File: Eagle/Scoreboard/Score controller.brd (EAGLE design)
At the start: 80 x 40.6 mm, 21 parts, among them IC3 74HC595N, Q1 BD437, Q2 BD437, Q3 BD437, Q4 BD437, Q5 BD437, Q6 BD437, Q7 BD437

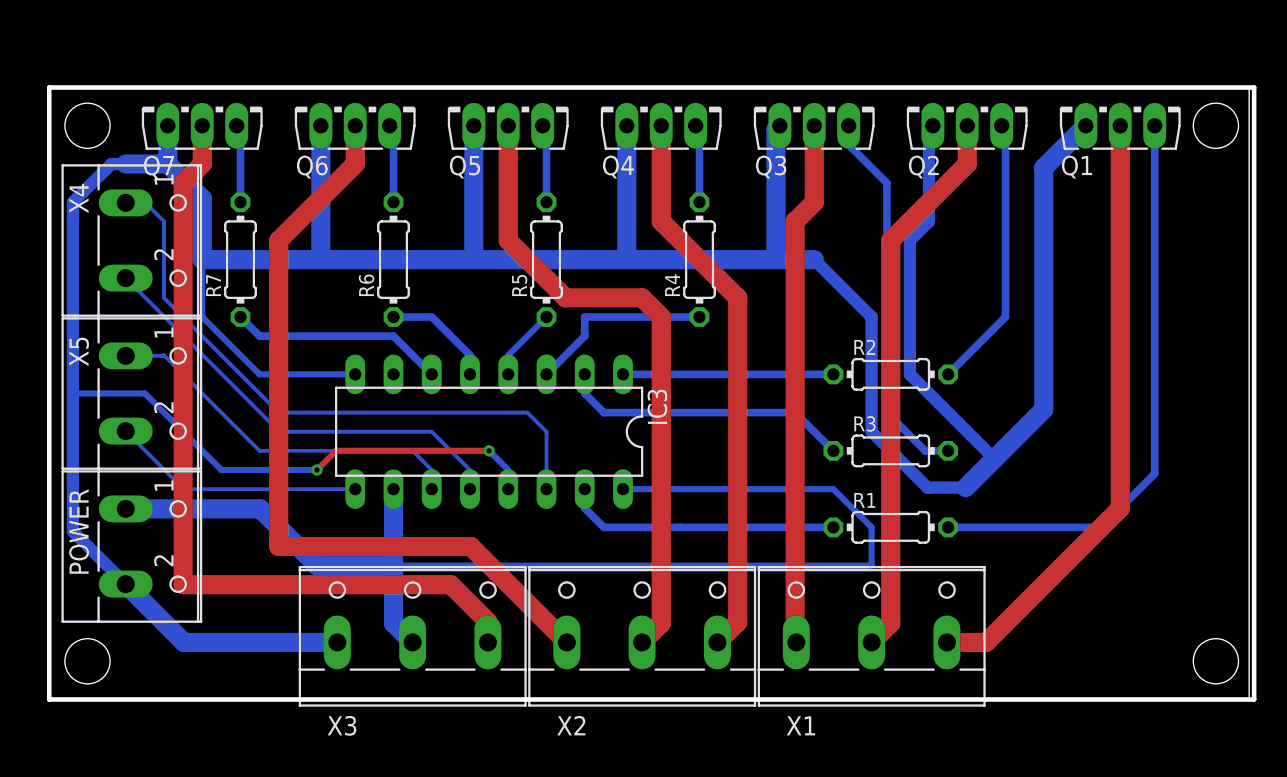
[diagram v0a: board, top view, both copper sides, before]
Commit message: Changed transistor type for score controller, changed number of terminals to 8. Motherboard still TBD
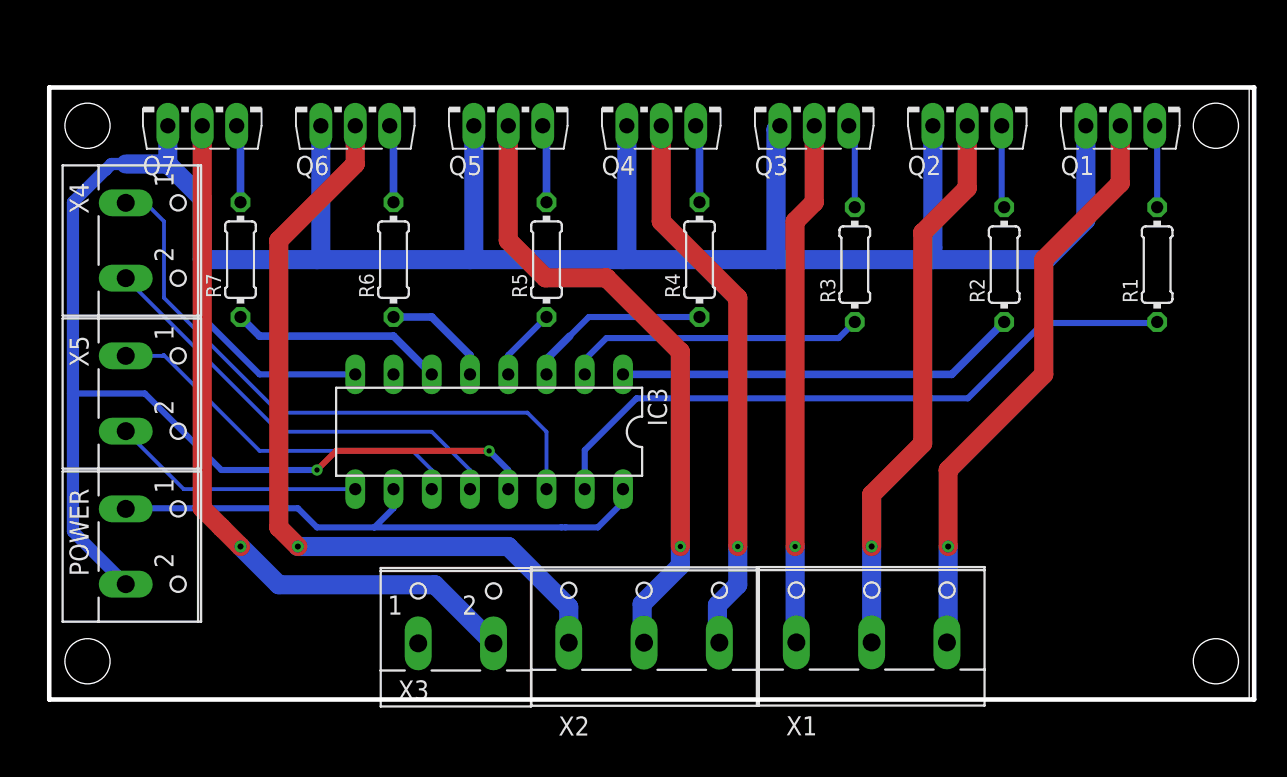
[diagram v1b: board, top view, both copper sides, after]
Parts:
- Q1, Q2, Q3, Q4, Q5, Q6, Q7: value BD437 -> BD237TO126AV; device transistor-power:TO126AV -> BD237:TO126V
- X3: device con-wago-500:W237-103 -> con-wago-500:W237-102
- moved R1 24.8 mm to (73.6, 28.9), turned to 90 degrees
- moved R3 12.6 mm to (53.5, 28.9), turned to 90 degrees
- moved R2 10.5 mm to (63.4, 28.9), turned to 90 degrees
- moved X3 2.87 mm to (27.0, 5.00)
- moved X2 0.13 mm to (39.5, 5.06)
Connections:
- net A: now also Q1.2; no longer Q1.C
- net B: now also Q2.2; no longer Q2.C
- net C: now also Q3.2; no longer Q3.C
- net D: now also Q4.2; no longer Q4.C
- net E: now also Q5.2; no longer Q5.C
- net F: now also Q6.2; no longer Q6.C
- net G: now also Q7.2, X3.2; no longer Q7.C, X3.3
- net GND: now also Q1.1, Q2.1, Q3.1, Q4.1, Q5.1, Q6.1, Q7.1; no longer Q1.E, Q2.E, Q3.E, Q4.E, Q5.E, Q6.E, Q7.E, X3.1
- net N$10: now also Q3.3; no longer Q3.B
- net N$11: now also Q4.3; no longer Q4.B
- net N$12: now also Q5.3; no longer Q5.B
- net N$13: now also Q6.3; no longer Q6.B
- net N$14: now also Q7.3; no longer Q7.B
- net N$2: now also Q1.3; no longer Q1.B
- net N$5: now also Q2.3; no longer Q2.B
- net VCC: no longer X3.2
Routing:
- net GND: track 258.4 -> 203.8 mm
- net VCC: track 81.9 -> 38.2 mm
- net N$2: track 38.3 -> 5.48 mm
- net N$4: track 18.3 -> 44.1 mm
- net N$10: track 25.2 -> 5.58 mm
- net N$1: track 14.0 -> 26.8 mm
- net N$5: track 18.2 -> 5.48 mm
- net G: track 53.6 -> 48.5 mm, vias 0 -> 1
- net A: track 40.6 -> 39.1 mm, vias 0 -> 1
- net F: track 51.8 -> 52.6 mm, vias 0 -> 1
- net N$3: track 19.4 -> 19.9 mm
- net E: track 42.0 -> 42.5 mm, vias 0 -> 1
- net D: vias 0 -> 1
- net C: vias 0 -> 1
- net B: vias 0 -> 1

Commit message: Chnaged all switch transistor to BC-337 TO92 AMMO
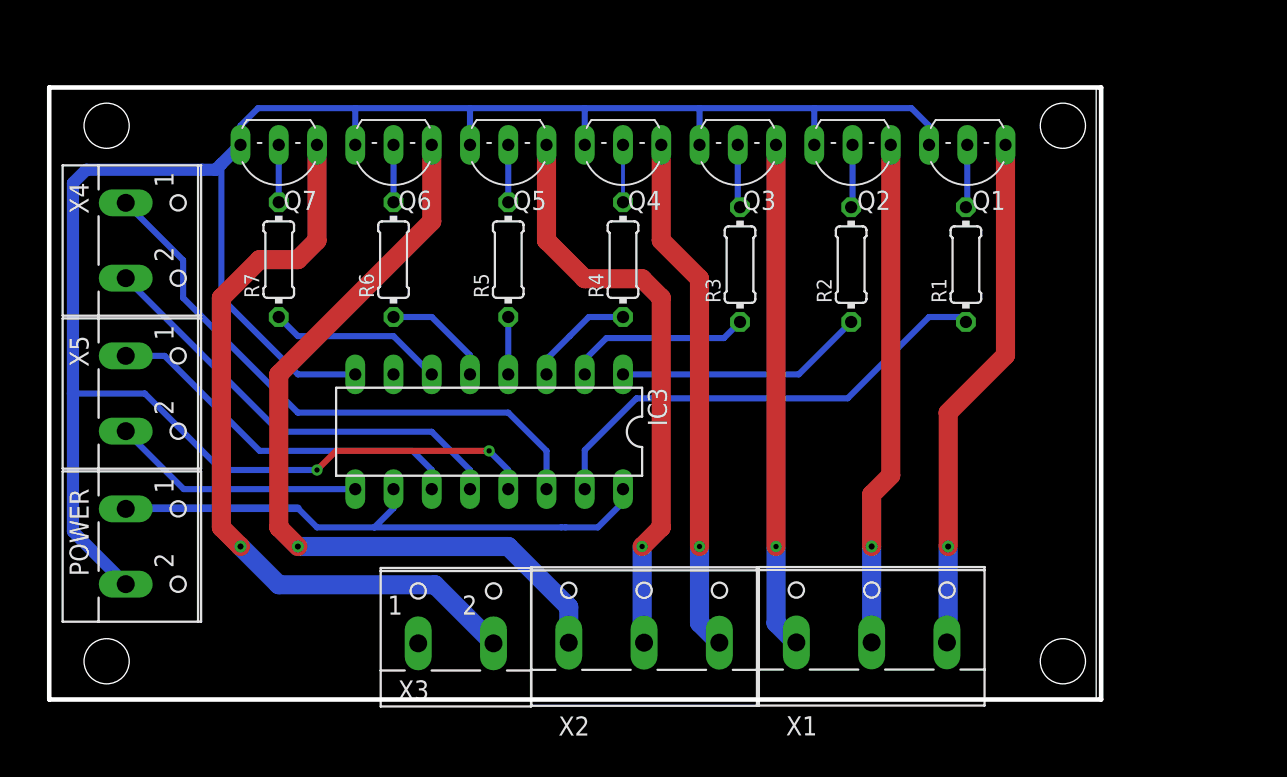
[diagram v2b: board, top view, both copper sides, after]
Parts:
- Q1, Q2, Q3, Q4, Q5, Q6, Q7: value BD237TO126AV -> BC338-40; device BD237:TO126V -> transistor-npn:TO92-EBC
- moved R1 12.7 mm to (60.9, 28.9)
- moved Q1 10.9 mm to (61.0, 35.6), turned to 180 degrees
- moved R2 10.2 mm to (53.2, 28.9)
- moved Q2 8.52 mm to (53.3, 35.6), turned to 180 degrees
- moved R3 7.62 mm to (45.9, 28.9)
- moved Q7 6.35 mm to (15.2, 35.6), turned to 180 degrees
- moved Q3 6.35 mm to (45.7, 35.6), turned to 180 degrees
- moved R4 5.08 mm to (38.1, 29.2)
- moved Q4 4.58 mm to (38.1, 35.6), turned to 180 degrees
- moved Q6 4.58 mm to (22.9, 35.6), turned to 180 degrees
- moved Q5 3.81 mm to (30.5, 35.6), turned to 180 degrees
- moved R5 2.54 mm to (30.5, 29.2)
- moved R7 2.54 mm to (15.2, 29.2)
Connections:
- net A: now also Q1.C; no longer Q1.2
- net B: now also Q2.C; no longer Q2.2
- net C: now also Q3.C; no longer Q3.2
- net D: now also Q4.C; no longer Q4.2
- net E: now also Q5.C; no longer Q5.2
- net F: now also Q6.C; no longer Q6.2
- net G: now also Q7.C; no longer Q7.2
- net GND: now also Q1.E, Q2.E, Q3.E, Q4.E, Q5.E, Q6.E, Q7.E; no longer Q1.1, Q2.1, Q3.1, Q4.1, Q5.1, Q6.1, Q7.1
- net N$10: now also Q3.B; no longer Q3.3
- net N$11: now also Q4.B; no longer Q4.3
- net N$12: now also Q5.B; no longer Q5.3
- net N$13: now also Q6.B; no longer Q6.3
- net N$14: now also Q7.B; no longer Q7.3
- net N$2: now also Q1.B; no longer Q1.3
- net N$5: now also Q2.B; no longer Q2.3
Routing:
- net GND: track 203.8 -> 154.9 mm
- net N$4: track 44.1 -> 31.7 mm
- net N$1: track 26.8 -> 16.6 mm
- net N$3: track 19.9 -> 12.3 mm
- net N$6: track 12.3 -> 7.24 mm
- net A: track 39.1 -> 34.7 mm
- net B: track 36.9 -> 33.6 mm
- net E: track 42.5 -> 39.2 mm
- net N$9: track 14.3 -> 11.7 mm
- net D: track 37.0 -> 34.7 mm
- net G: track 48.5 -> 50.8 mm
- net DS: track 41.0 -> 38.8 mm
- net C: track 34.9 -> 33.5 mm
- net N$10: track 5.58 -> 4.20 mm
- net N$12: track 5.19 -> 3.81 mm
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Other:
- board size 80 x 40.6 mm -> 69.8 x 40.6 mm

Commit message: Added polygons
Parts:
- moved R1 0.35 mm to (61.0, 29.2)
- moved R2 0.35 mm to (53.4, 29.2)
- moved R3 0.35 mm to (45.7, 29.2)
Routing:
- added copper zone on layer 1, net GND
- added copper zone on layer 16, net GND

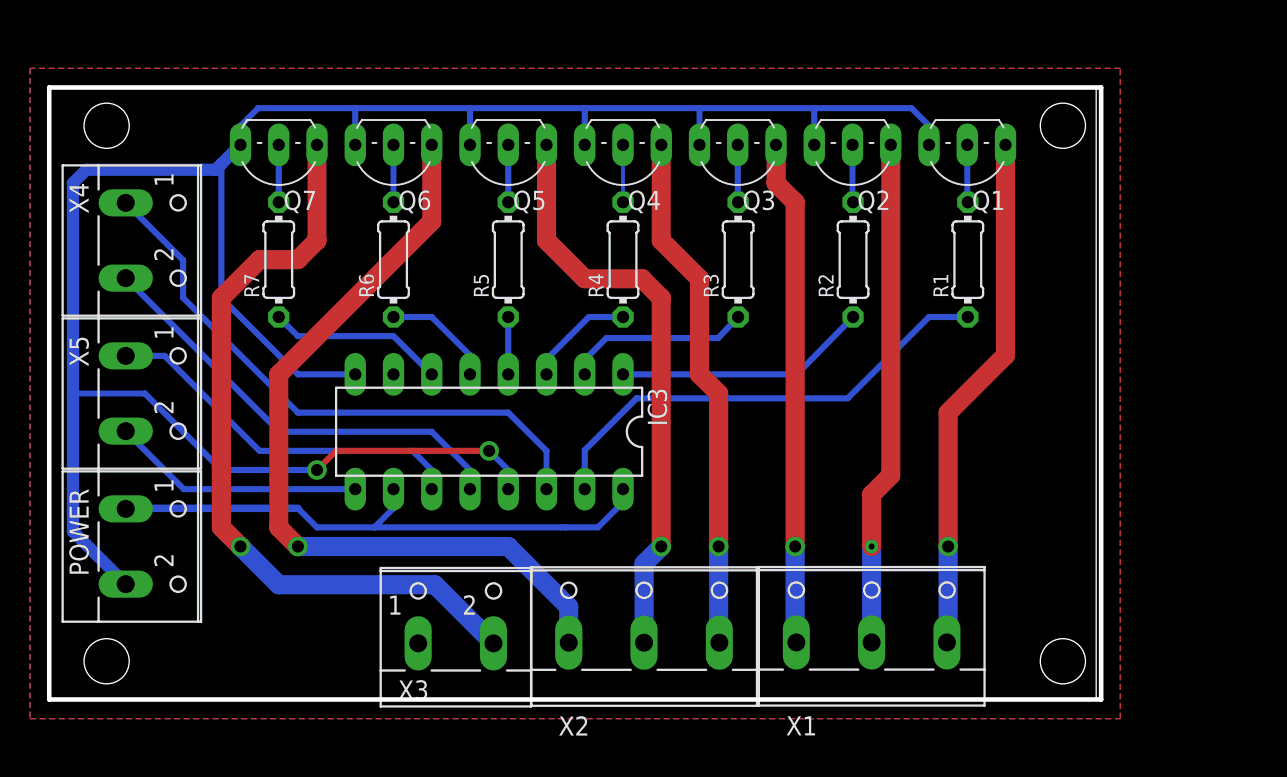
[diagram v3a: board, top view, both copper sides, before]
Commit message: Changed the board to be just one layer
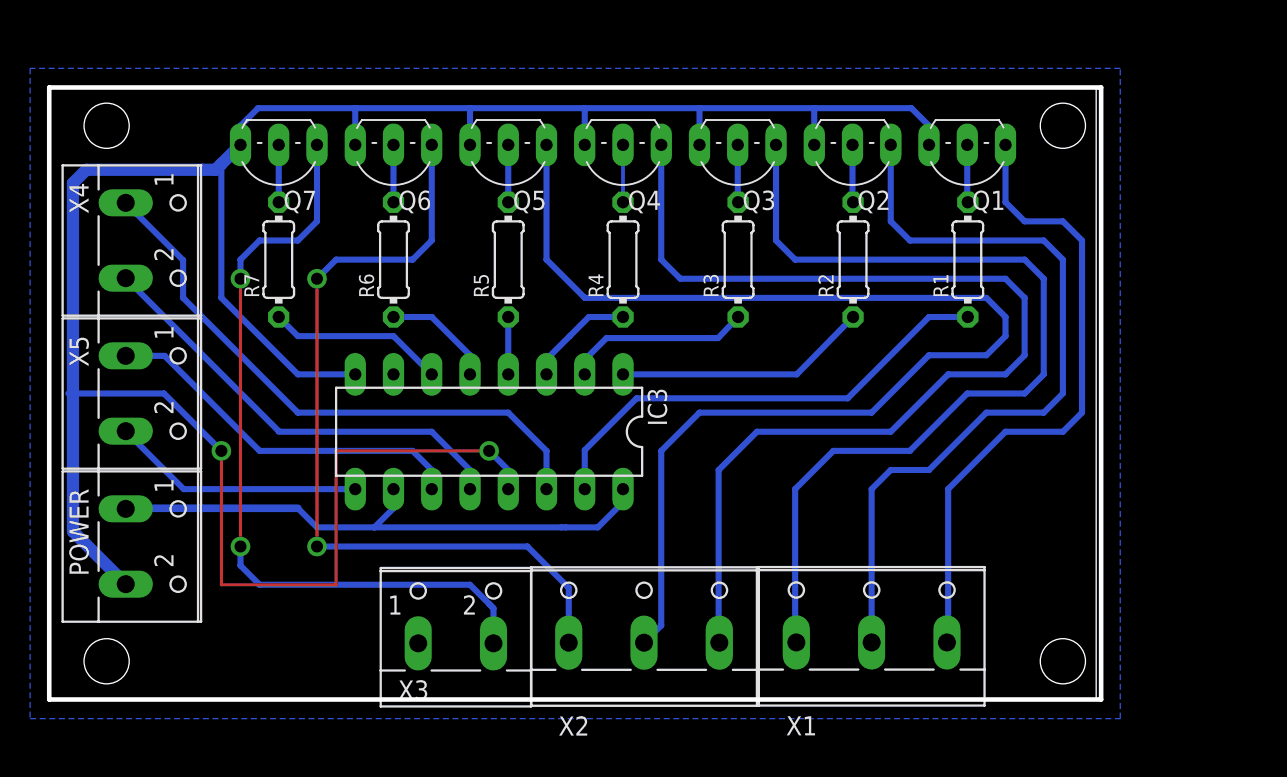
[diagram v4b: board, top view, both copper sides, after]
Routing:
- net E: track 38.9 -> 80.2 mm, vias 1 -> 0
- net D: track 34.7 -> 71.5 mm, vias 1 -> 0
- net C: track 33.6 -> 61.4 mm, vias 1 -> 0
- net B: track 33.6 -> 52.0 mm, vias 1 -> 0
- net GND: track 154.9 -> 171.9 mm
- net A: track 34.7 -> 42.6 mm, vias 1 -> 0
- net G: track 50.8 -> 52.2 mm, vias 1 -> 2
- net F: track 53.4 -> 54.3 mm, vias 1 -> 2
- removed copper zone on layer 1, net GND

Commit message: Added more space for screws
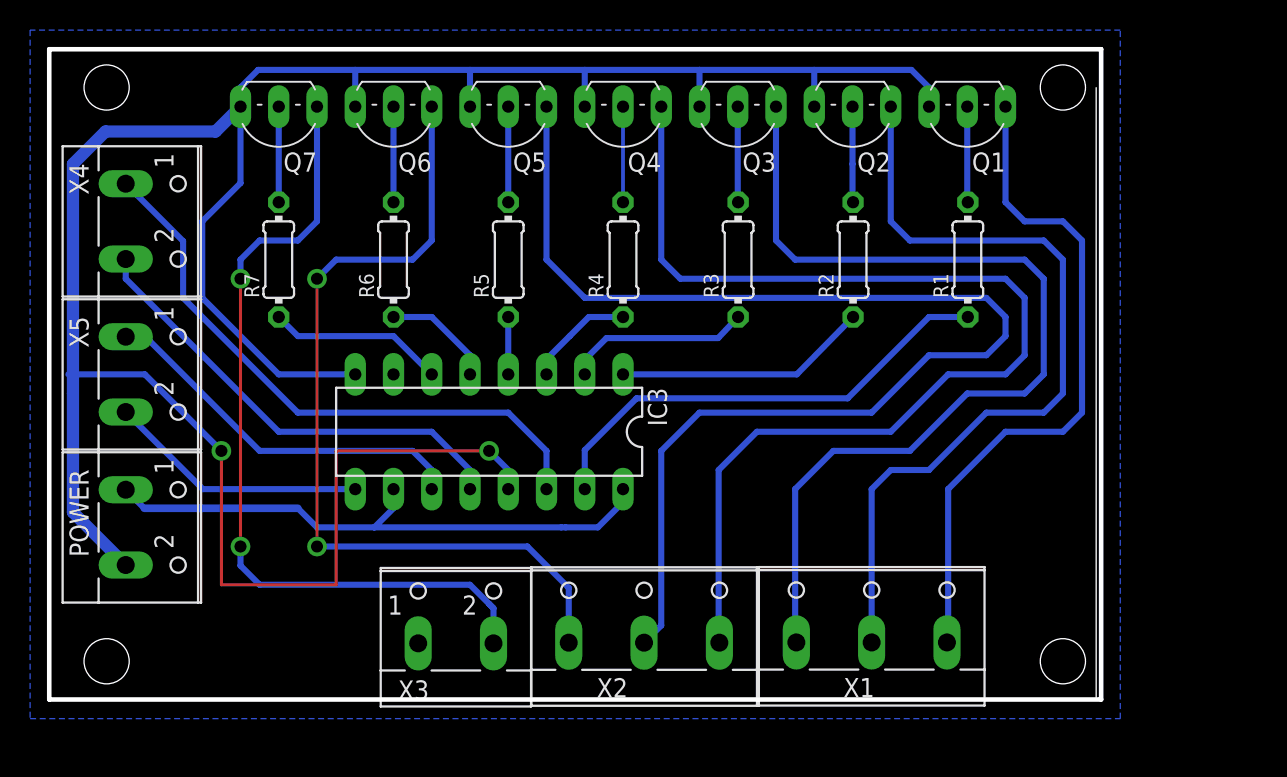
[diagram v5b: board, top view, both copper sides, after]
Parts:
- moved Q1 2.54 mm to (61.0, 38.1)
- moved Q2 2.54 mm to (53.3, 38.1)
- moved Q3 2.54 mm to (45.7, 38.1)
- moved Q4 2.54 mm to (38.1, 38.1)
- moved Q5 2.54 mm to (30.5, 38.1)
- moved Q6 2.54 mm to (22.9, 38.1)
- moved Q7 2.54 mm to (15.2, 38.1)
- moved POWER 1.27 mm to (6.35, 11.4)
- moved X4 1.27 mm to (6.35, 31.8)
- moved X5 1.27 mm to (6.35, 21.6)
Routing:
- net GND: track 171.9 -> 180.1 mm
- net E: track 80.2 -> 82.7 mm
- net D: track 71.5 -> 74.1 mm
- net N$2: track 4.15 -> 6.69 mm
- net N$14: track 3.81 -> 6.35 mm
- net N$13: track 3.81 -> 6.35 mm
- net N$12: track 3.81 -> 6.35 mm
- net N$11: track 3.81 -> 6.35 mm
- net G: track 52.2 -> 54.7 mm
- net C: track 61.4 -> 64.0 mm
- net B: track 52.0 -> 54.5 mm
- net A: track 42.6 -> 45.1 mm
- net N$10: track 3.92 -> 6.46 mm
- net F: track 54.3 -> 56.8 mm
- net N$5: track 3.90 -> 6.37 mm
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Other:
- board size 69.8 x 40.6 mm -> 69.8 x 43.2 mm
